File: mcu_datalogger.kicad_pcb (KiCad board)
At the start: 2 copper layers, 29 parts, among them J1 Conn_01x04_Pin, J2 Conn_01x04_Pin, J3 Conn_01x09_Pin, J4 Conn_02x03_Odd_Even, U1 24LC1025, U2 24LC1025, U3 DS1337S_, U4 ATMEGA328P-AU, Y1 32.768, Y2 16 MHz

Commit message: initial pcb layout
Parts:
- moved J3 60.1 mm to (105.4, 103.0), turned to 90 degrees
- moved J2 48.5 mm to (130.9, 103.0), turned to 90 degrees
- moved Y1 40.5 mm to (102.0, 92.6), turned to 90 degrees
- moved H3 39.1 mm to (100.5, 102.2)
- moved BT1 34.7 mm to (102.0, 84.0), turned to 180 degrees
- moved H1 32.1 mm to (100.7, 76.0)
- moved U3 29.5 mm to (110.0, 93.0)
- moved J1 27.2 mm to (146.0, 90.4)
- moved U4 24.7 mm to (123.0, 86.0)
- moved Y2 23.6 mm to (119.4, 94.5)
- moved R1 23.0 mm to (109.0, 98.5), turned to 180 degrees
- moved H4 22.9 mm to (145.1, 102.3)
- moved R6 21.7 mm to (134.6, 77.0)
- moved R5 20.4 mm to (139.6, 83.9), turned to -90 degrees
- moved R7 18.5 mm to (136.7, 87.8), turned to 90 degrees
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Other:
- board outline added: 50.2 x 32.1 mm

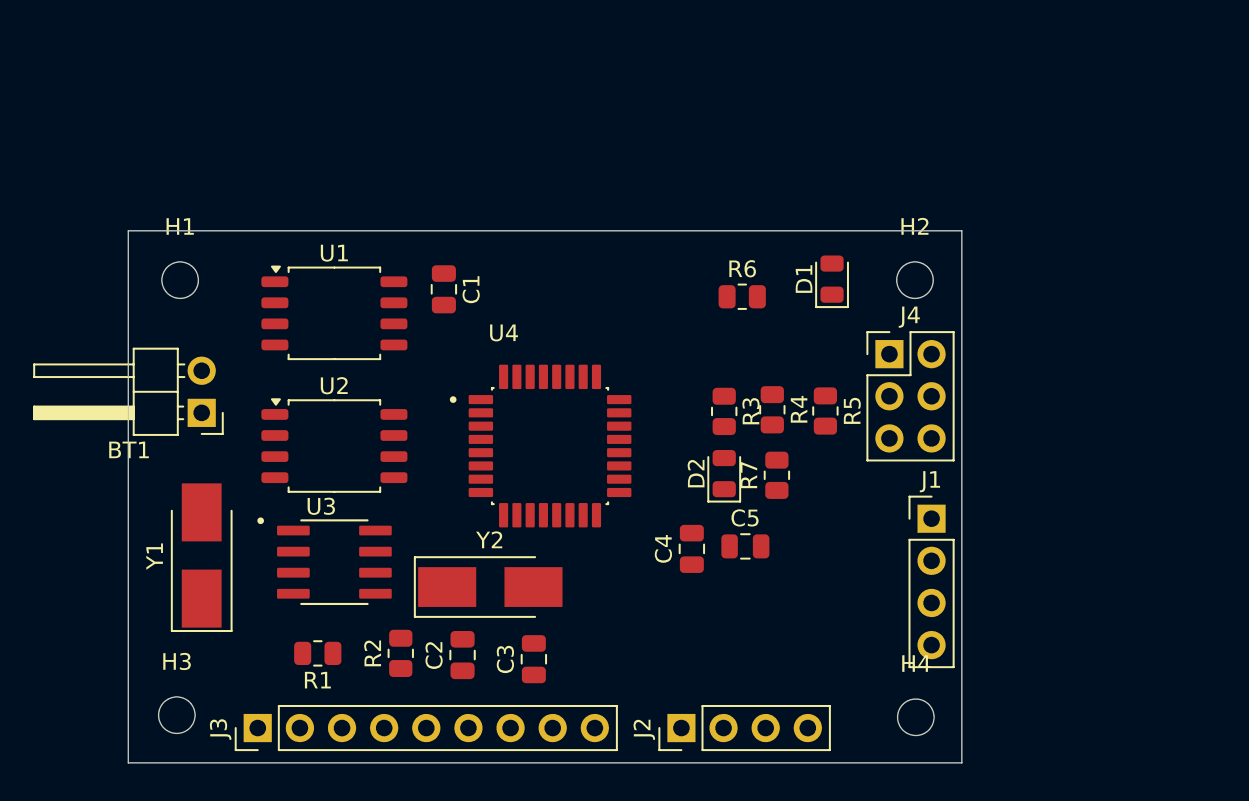
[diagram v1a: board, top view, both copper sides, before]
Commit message: re-arranged footprints
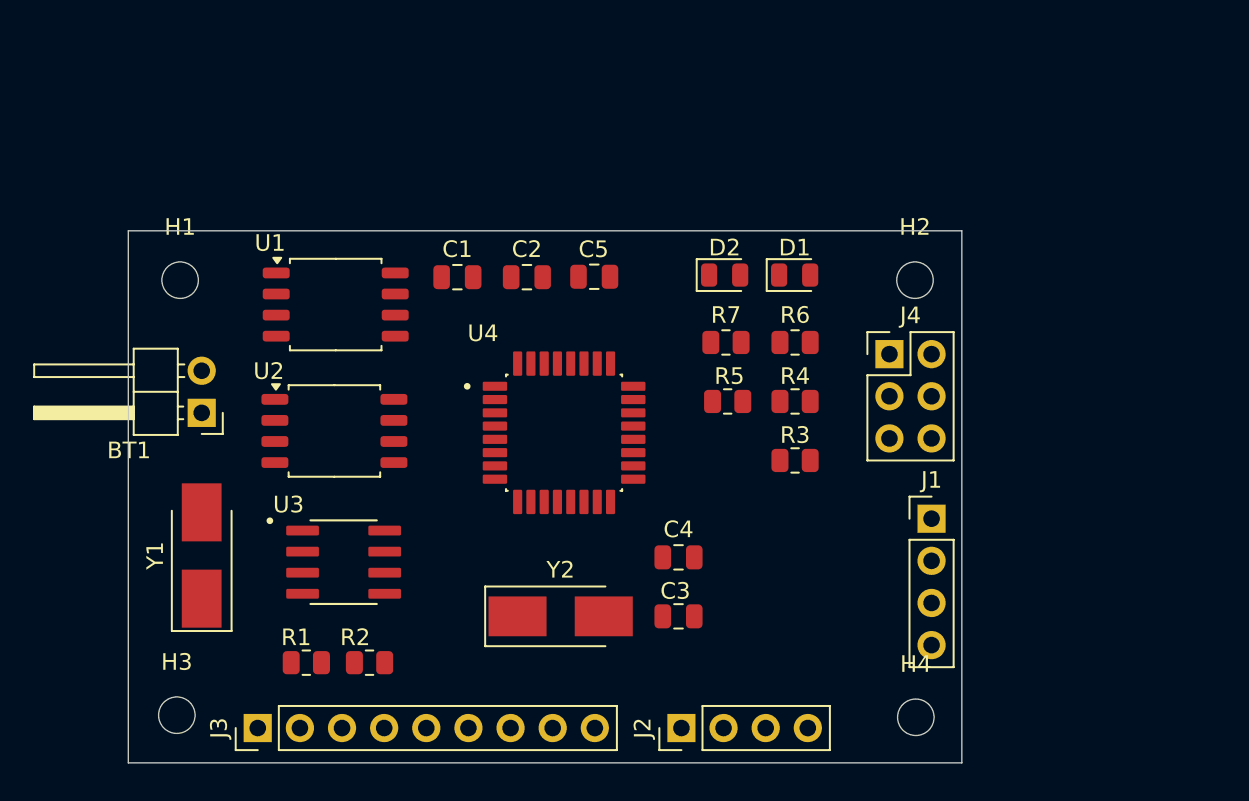
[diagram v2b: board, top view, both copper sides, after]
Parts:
- moved C2 23.1 mm to (121.6, 75.8), turned to 0 degrees
- moved C5 18.6 mm to (125.7, 75.8), turned to 180 degrees
- moved D2 12.0 mm to (133.5, 75.7), turned to 0 degrees
- moved C3 9.09 mm to (130.7, 96.3), turned to 180 degrees
- moved R7 8.58 mm to (133.6, 79.8), turned to 0 degrees
- moved R5 5.92 mm to (133.7, 83.3), turned to 180 degrees
- moved R3 5.19 mm to (137.8, 86.9), turned to 180 degrees
- moved Y2 4.59 mm to (123.6, 96.3)
- moved R6 4.21 mm to (137.8, 79.8)
- moved D1 2.27 mm to (137.7, 75.7), turned to 0 degrees
- moved R2 1.96 mm to (112.1, 99.1), turned to 0 degrees
- moved R4 1.46 mm to (137.8, 83.3), turned to 180 degrees
- moved U4 1.17 mm to (123.8, 85.2)
- moved C1 1.09 mm to (117.4, 75.8), turned to 0 degrees
- moved C4 0.95 mm to (130.7, 92.7), turned to 0 degrees
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
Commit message: begin routing top layer
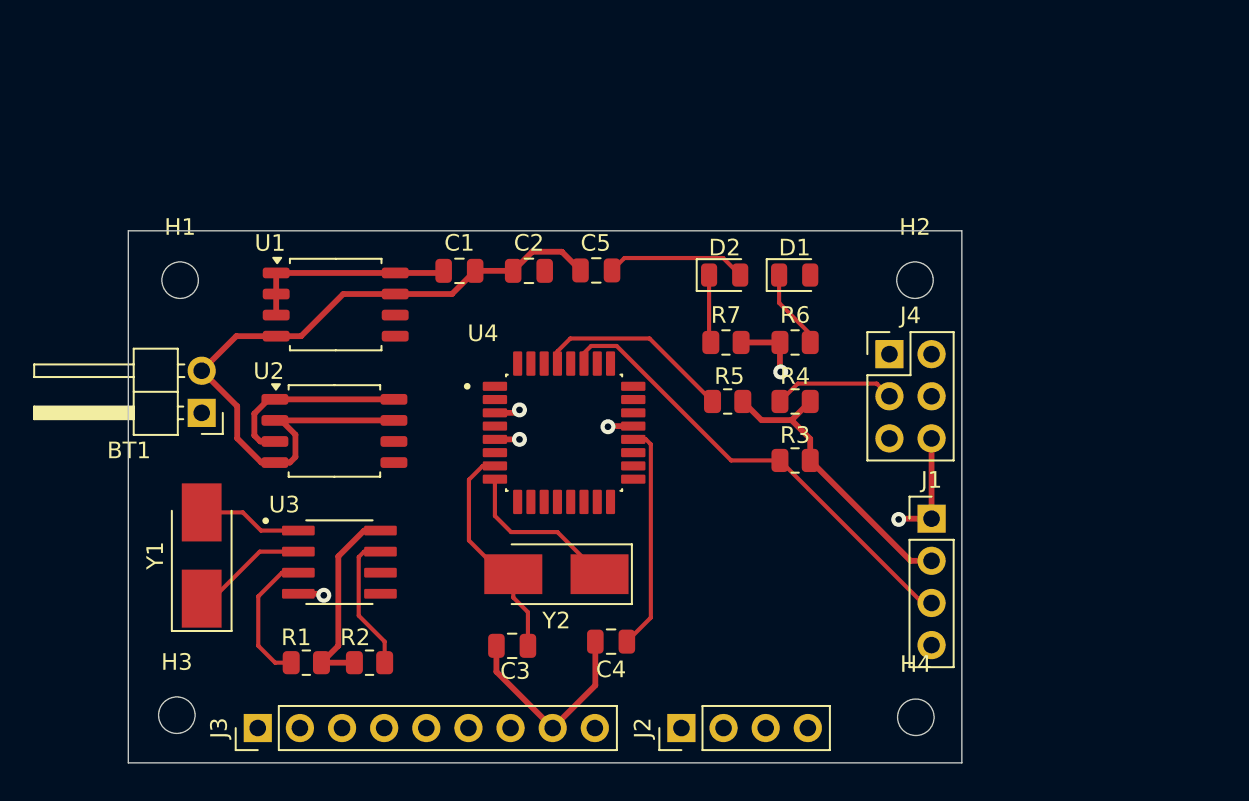
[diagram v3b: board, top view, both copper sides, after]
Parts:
- moved C3 10.2 mm to (120.7, 98.0), turned to 0 degrees
- moved C4 6.51 mm to (126.7, 97.8), turned to 180 degrees
- moved Y2 2.55 mm to (123.4, 93.7), turned to 180 degrees
- moved C1 0.40 mm to (117.5, 75.4)
- moved C2 0.40 mm to (121.7, 75.4)
- moved C5 0.40 mm to (125.8, 75.4)
- moved U3 0.25 mm to (110.3, 93.0)
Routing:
- net GND: track 0.00 -> 75.4 mm, vias 0 -> 6
- net /Vcc: track 0.00 -> 54.1 mm
- net /SDA: track 0.00 -> 28.2 mm
- net Net-(U4-PB6): track 0.00 -> 13.8 mm
- net Net-(U4-AREF): track 0.00 -> 13.7 mm
- net /RESET: track 0.00 -> 12.0 mm
- net Net-(U4-PB7): track 0.00 -> 9.98 mm
- net Net-(U3-SQW/~INT): track 0.00 -> 8.46 mm
- net Net-(BT1-+): track 0.00 -> 8.46 mm
- net Net-(U3-~{INTA}): track 0.00 -> 8.39 mm
- net /SCK: track 0.00 -> 7.94 mm
- net Net-(U3-X2): track 0.00 -> 7.00 mm
- net Net-(U3-X1): track 0.00 -> 6.28 mm
- net Net-(D1-K): track 0.00 -> 4.84 mm
- net Net-(D2-K): track 0.00 -> 4.11 mm

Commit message: routed
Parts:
- moved J2 27.5 mm to (129.3, 75.6), turned to -90 degrees
- moved D2 17.9 mm to (116.9, 82.4)
- moved R7 17.8 mm to (116.9, 86.1)
- moved D1 16.1 mm to (131.9, 90.7), turned to 90 degrees
- moved C2 15.2 mm to (117.3, 90.0), turned to 90 degrees
- moved C4 13.6 mm to (130.8, 84.8), turned to 90 degrees
- moved R6 11.5 mm to (134.7, 90.8), turned to -90 degrees
- moved R5 10.5 mm to (124.5, 78.4)
- moved C5 9.58 mm to (116.9, 79.0)
- moved R3 9.27 mm to (131.1, 80.5)
- moved R4 5.33 mm to (134.2, 87.3)
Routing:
- net /Vcc: track 54.1 -> 140.1 mm
- net /SCK: track 7.94 -> 81.4 mm, vias 0 -> 3
- net /SDA: track 28.2 -> 83.6 mm, vias 0 -> 3
- net GND: track 75.4 -> 32.8 mm, vias 6 -> 18
- net /D2: track 0.00 -> 30.3 mm, vias 0 -> 2
- net /D4: track 0.00 -> 29.7 mm, vias 0 -> 2
- net /D3: track 0.00 -> 27.2 mm, vias 0 -> 2
- net Net-(BT1-+): track 8.46 -> 33.7 mm
- net /MOSI: track 0.00 -> 24.9 mm, vias 0 -> 2
- net /MISO: track 0.00 -> 20.5 mm, vias 0 -> 2
- net /D6: track 0.00 -> 17.1 mm, vias 0 -> 2
- net /D5: track 0.00 -> 17.0 mm, vias 0 -> 2
- net /RESET: track 12.0 -> 28.5 mm, vias 0 -> 2
- net /D8: track 0.00 -> 15.6 mm, vias 0 -> 2
- net /D7: track 0.00 -> 15.5 mm, vias 0 -> 2
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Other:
- board size 50.2 x 32.1 mm -> 51 x 32.1 mm

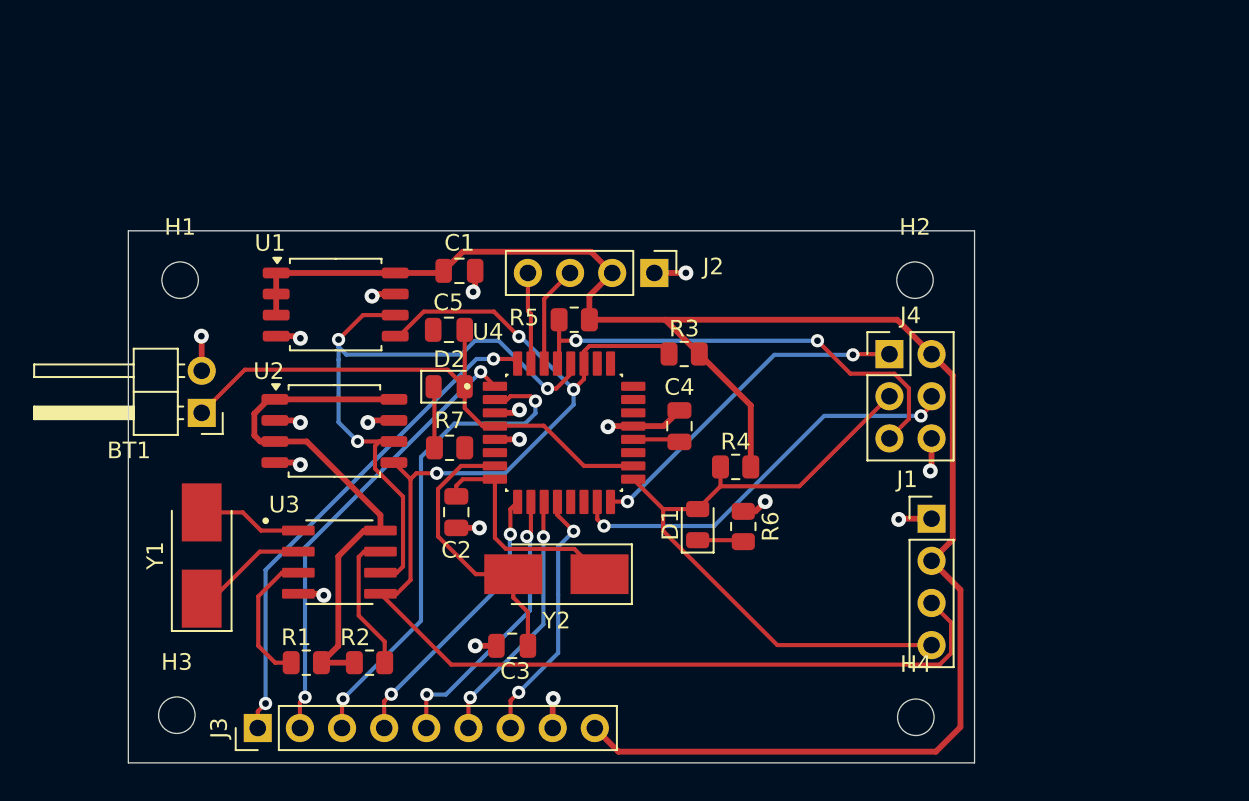
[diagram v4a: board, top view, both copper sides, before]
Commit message: copper fills added
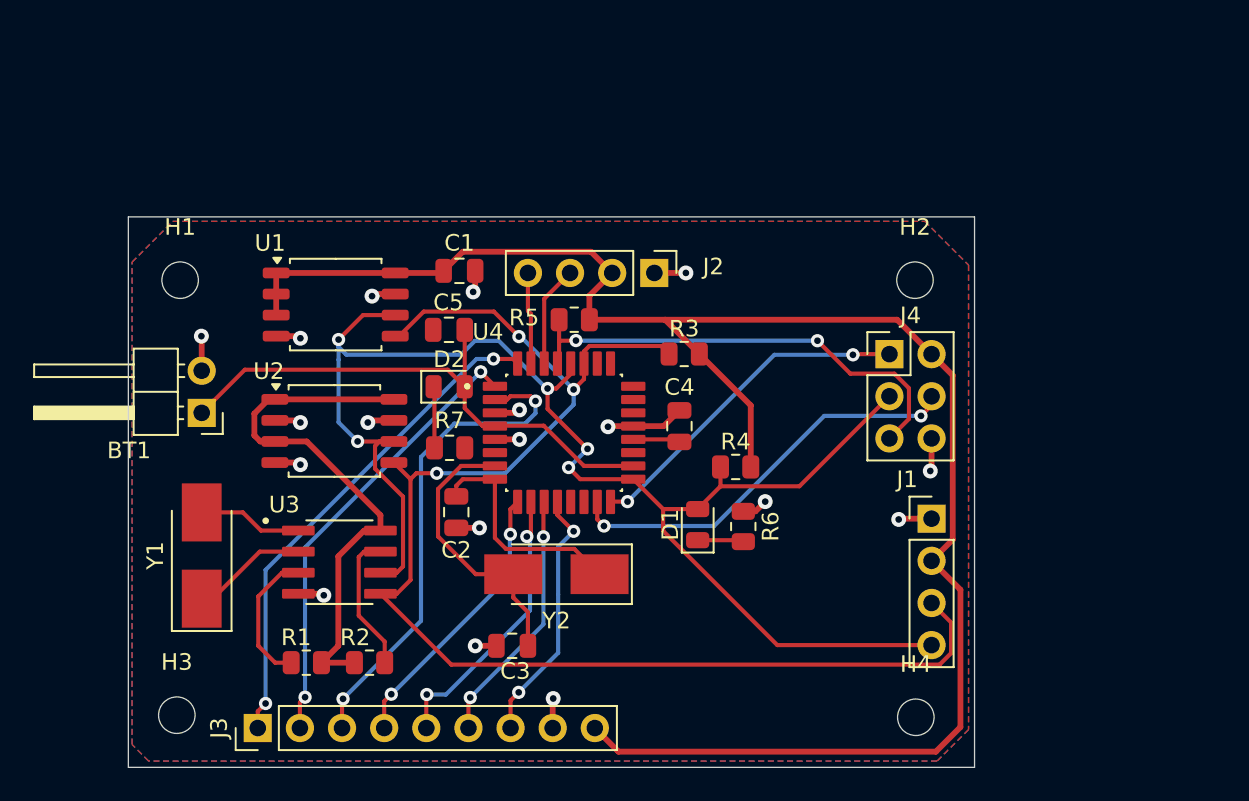
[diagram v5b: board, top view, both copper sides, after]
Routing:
- net /SCK: track 81.4 -> 91.8 mm, vias 3 -> 5
- added copper zone on F.Cu, net /Vcc
- added copper zone on B.Cu, net GND
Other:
- board size 51 x 32.1 mm -> 51 x 33.2 mm
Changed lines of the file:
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@@
 	)
 	(gr_rect
-		(start 97.578 73.025)
-		(end 148.59 105.1)
+		(start 97.578 72.185)
+		(end 148.59 105.37)
 		(stroke
 			(width 0.05)
@@
 	)
 	(segment
+		(start 122.85 83.76)
+		(end 122.85 82.53)
+		(width 0.25)
+		(layer "F.Cu")
+		(net 7)
+	)
+	(segment
 		(start 146 98)
 		(end 136.7 98)
@@
 	)
 	(segment
+		(start 124.818694 87.998)
+		(end 124.115347 87.294653)
+		(width 0.25)
+		(layer "F.Cu")
+		(net 7)
+	)
+	(segment
 		(start 113.761 93.635)
 		(end 114.137 93.259)
@@
 	)
 	(segment
+		(start 125.26 86.17)
+		(end 122.85 83.76)
+		(width 0.25)
+		(layer "F.Cu")
+		(net 7)
+	)
+	(segment
 		(start 131.9 89.8)
 		(end 129.818 89.8)
@@
 	)
 	(segment
+		(start 128.016 87.998)
+		(end 124.818694 87.998)
+		(width 0.25)
+		(layer "F.Cu")
+		(net 7)
+	)
+	(segment
 		(start 133.275 88.425)
 		(end 131.9 89.8)
@@
 	)
 	(via
+		(at 124.115347 87.294653)
+		(size 0.8)
+		(drill 0.4)
+		(layers "F.Cu" "B.Cu")
+		(net 7)
+	)
+	(via
+		(at 125.26 86.17)
+		(size 0.8)
+		(drill 0.4)
+		(layers "F.Cu" "B.Cu")
+		(net 7)
+	)
+	(via
 		(at 110.25 79.58)
 		(size 0.8)
@@
 	)
 	(segment
+		(start 124.115347 87.294653)
+		(end 124.135347 87.294653)
+		(width 0.25)
+		(layer "B.Cu")
+		(net 7)
+	)
+	(segment
 		(start 110.25 84.57)
 		(end 110.25 80.8)
@@
 	)
 	(segment
+		(start 124.135347 87.294653)
+		(end 125.26 86.17)
+		(width 0.25)
+		(layer "B.Cu")
+		(net 7)
+	)
+	(segment
 		(start 110.72 80.49)
 		(end 117.64 80.49)
@@
 		(net 26)
 	)
+	(zone
+		(net 3)
+		(net_name "/Vcc")
+		(layer "F.Cu")
+		(hatch edge 0.5)
+		(connect_pads
+			(clearance 0.5)
+		)
+		(min_thickness 0.25)
+		(filled_areas_thickness no)
+		(fill yes
+			(mode hatch)
+			(thermal_gap 0.5)
+			(thermal_bridge_width 0.5)
+			(hatch_thickness 1)
+			(hatch_gap 1.5)
+			(hatch_orientation 0)
+			(hatch_border_algorithm hatch_thickness)
+			(hatch_min_hole_area 0.3)
+		)
+		(polygon
+			(pts
+				(xy 148.23 75.09) (xy 148.23 103.09) (xy 146.33 104.99) (xy 98.8 104.99) (xy 97.8 103.99) (xy 97.8 74.91)
+				(xy 100.26 72.45) (xy 145.59 72.45)
+			)
+		)
+	)
+	(zone
+		(net 2)
+		(net_name "GND")
+		(layer "B.Cu")
+		(hatch edge 0.5)
+		(connect_pads
+			(clearance 0.5)
+		)
+		(min_thickness 0.25)
+		(filled_areas_thickness no)
+		(fill yes
+			(mode hatch)
+			(thermal_gap 0.5)
+			(thermal_bridge_width 0.5)
+			(hatch_thickness 1)
+			(hatch_gap 1.5)
+			(hatch_orientation 0)
+			(hatch_border_algorithm hatch_thickness)
+			(hatch_min_hole_area 0.3)
+		)
+		(polygon
+			(pts
+				(xy 148.23 75.09) (xy 148.23 103.09) (xy 146.33 104.99) (xy 98.8 104.99) (xy 97.8 103.99) (xy 97.8 74.91)
+				(xy 100.26 72.45) (xy 145.59 72.45)
+			)
+		)
+	)
 	(embedded_fonts no)
